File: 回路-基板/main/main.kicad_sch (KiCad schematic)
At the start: 45 parts, among them J2 Conn_01x06_Pin, Q1 PNP, Q2 NPN, Q3 PNP, Q4 NPN, SW1 SW_Push, SW2 SW_Push, SW3 SW_Push, SW4 SW_Push, SW5 SW_Push, SW6 SW_SPDT, U1 TWE-L-WX, U3 LM1117MP-3.3

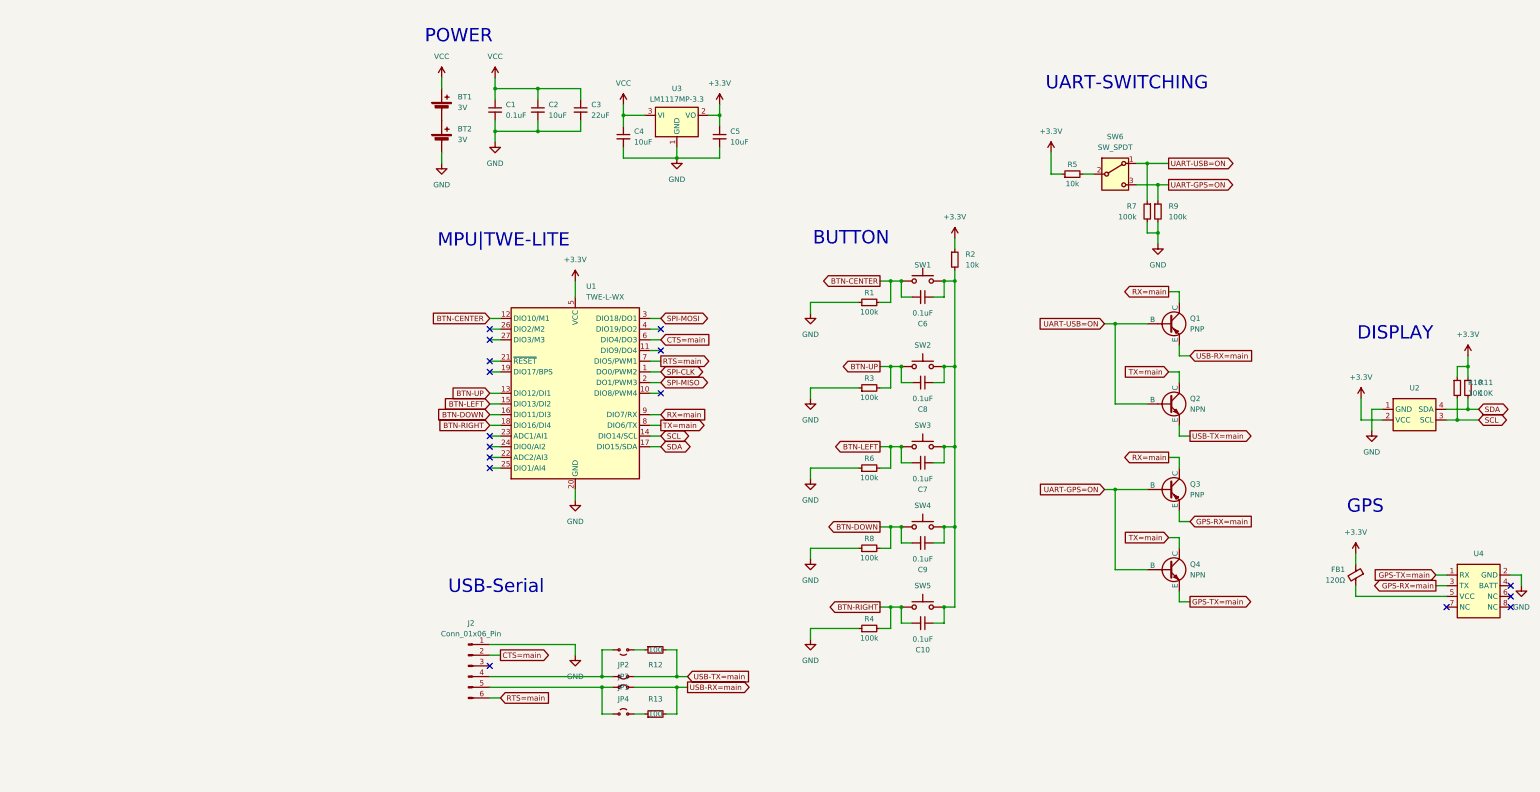
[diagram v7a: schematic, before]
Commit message: 子機基板の回路図を更新した
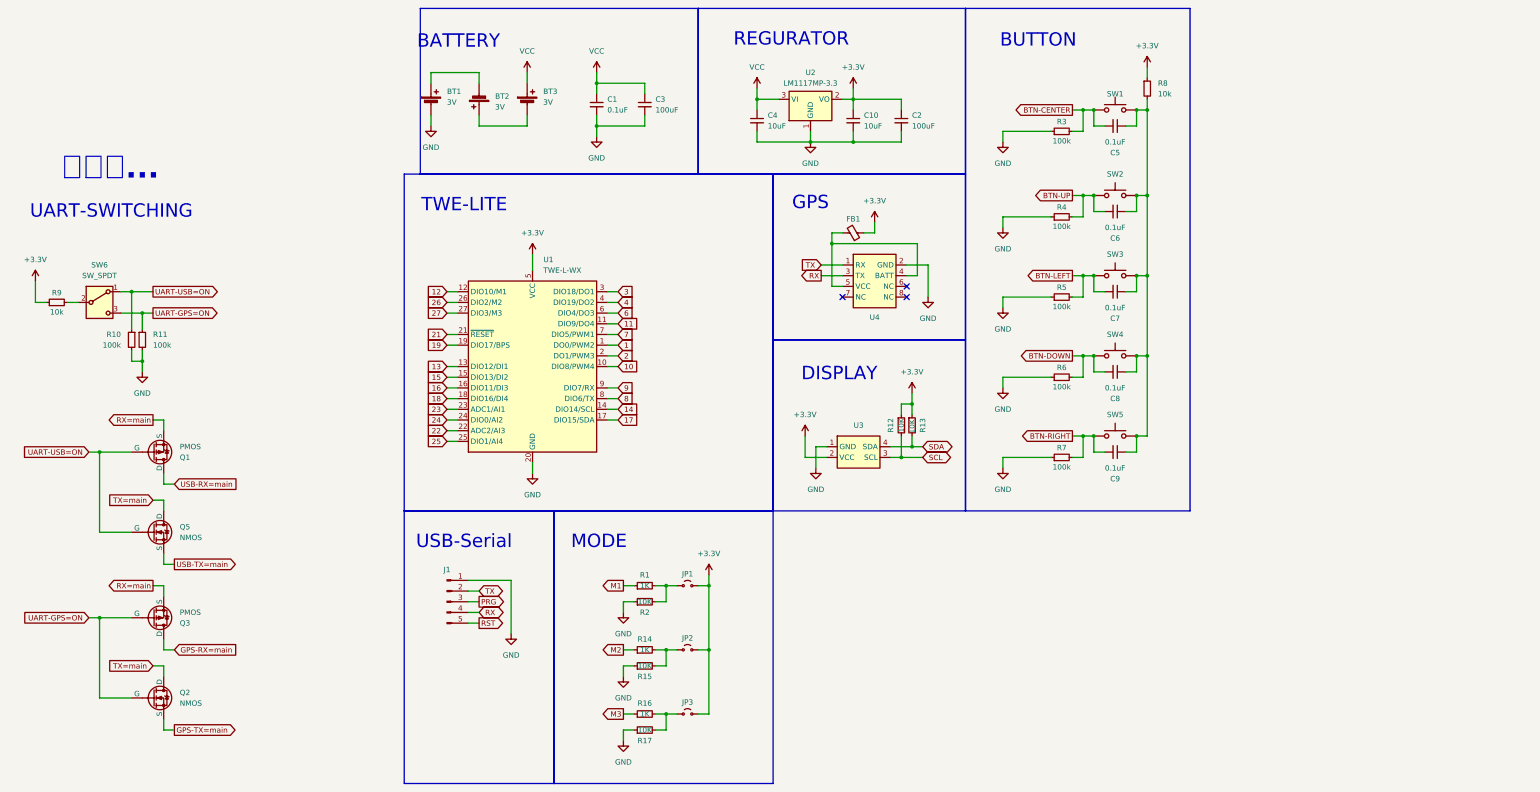
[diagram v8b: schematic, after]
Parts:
- removed J2: Conn_01x06_Pin, Connector_PinSocket_2.54mm:PinSocket_1x06_P2.54mm_Horizontal, symbol Connector:Conn_01x06_Pin
- removed JP1, JP3: Jumper_2_Small_Bridged, Jumper:SolderJumper-2_P1.3mm_Bridged_Pad1.0x1.5mm, symbol Jumper:Jumper_2_Small_Bridged
- removed JP4: Jumper_2_Small_Open, Jumper:SolderJumper-2_P1.3mm_Open_Pad1.0x1.5mm, symbol Jumper:Jumper_2_Small_Open
- removed Q1, Q3: PNP, Package_TO_SOT_SMD:SOT-323_SC-70, symbol Simulation_SPICE:PNP
- removed Q2, Q4: NPN, Package_TO_SOT_SMD:SC-59, symbol Simulation_SPICE:NPN
- removed R12, R13: 100, Resistor_SMD:R_0805_2012Metric, symbol Device:R_Small
- added BT3: 3V, @2024-cansat:BHSD-2032-SM, symbol Device:Battery_Cell
- added J1: Conn_01x05_Pin, symbol Connector:Conn_01x05_Pin
- added JP1, JP3: Jumper_2_Small_Open, symbol Jumper:Jumper_2_Small_Open
- added Q1, Q3: PMOS, symbol Simulation_SPICE:PMOS
- added Q2, Q5: NMOS, symbol Simulation_SPICE:NMOS
- added R1, R14, R16: 1K, symbol Device:R_Small
- added R15, R17, R2: 10K, symbol Device:R_Small
- C2: value 10uF -> 100uF
- C3: value 22uF -> 100uF
- FB1: value 120Ω -> FerriteBead_Small; footprint Inductor_SMD:L_0603_1608Metric -> (none)
- JP2: footprint Jumper:SolderJumper-2_P1.3mm_Open_Pad1.0x1.5mm -> (none)
- renumbered BT2 to BT1, BT1 to BT2, C5 to C10, C6 to C5, C8 to C6, C9 to C8, C10 to C9, R7 to R10, R9 to R11, R10 to R12, R11 to R13, R1 to R3, R3 to R4, R6 to R5, R8 to R6, R4 to R7, R2 to R8, R5 to R9, U3 to U2, U2 to U3
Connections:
- net +3.3V: now also C2.1, JP2.2 (B), JP1.2 (B), JP3.2 (B)
- net BTN-CENTER: no longer U1.12 (DIO10/M1)
- net BTN-DOWN: no longer U1.16 (DIO11/DI3)
- net BTN-LEFT: no longer U1.15 (DIO13/DI2)
- net BTN-RIGHT: no longer U1.18 (DIO16/DI4)
- net BTN-UP: no longer U1.13 (DIO12/DI1)
- net GND: now also J1.1 (Pin_1), R15.1, R17.1, R2.1
- net GPS-RX=main: now also Q3.1 (D); no longer U4.3 (TX)
- net GPS-TX=main: now also Q2.3 (S); no longer U4.1 (RX)
- net RX=main: now also Q1.3 (S), Q3.3 (S); no longer U1.9 (DIO7/RX)
- net SCL: no longer U1.14 (DIO14/SCL)
- net SDA: no longer U1.17 (DIO15/SDA)
- net TX=main: now also Q2.1 (D), Q5.1 (D); no longer U1.8 (DIO6/TX)
- net UART-GPS=ON: now also Q2.2 (G), Q3.2 (G)
- net UART-USB=ON: now also Q1.2 (G), Q5.2 (G)
- net USB-RX=main: now also Q1.1 (D)
- net USB-TX=main: now also Q5.3 (S)
- net VCC: now also BT3.1 (+); no longer BT2.1 (+), C2.1
- net 10: now reaches U1.10 (DIO8/PWM4)
- net 11: now reaches U1.11 (DIO9/DO4)
- net 19: now reaches U1.19 (DIO17/BPS)
- net 21: now reaches U1.21 (~{RESET})
- net 22: now reaches U1.22 (ADC2/AI3)
- net 23: now reaches U1.23 (ADC1/AI1)
- net 24: now reaches U1.24 (DIO0/AI2)
- net 25: now reaches U1.25 (DIO1/AI4)
- net 26: now reaches U1.26 (DIO2/M2)
- net 27: now reaches U1.27 (DIO3/M3)
- net 4: now reaches U1.4 (DIO19/DO2)
- net at JP2.1 (A): now also R14.2, R15.2
- net at FB1.2, U4.5 (VCC): now also U4.4 (BATT)
- net CTS=main renamed 6
- net RTS=main renamed 7
- net SPI-CLK renamed 1
- net SPI-MISO renamed 2
- net SPI-MOSI renamed 3
- new net: BT2.1 (+), BT3.2 (-)
- new net: JP1.1 (A), R1.2, R2.2
- new net: JP3.1 (A), R16.2, R17.2
- new net 12: U1.12 (DIO10/M1)
- new net 13: U1.13 (DIO12/DI1)
- new net 14: U1.14 (DIO14/SCL)
- new net 15: U1.15 (DIO13/DI2)
- new net 16: U1.16 (DIO11/DI3)
- new net 17: U1.17 (DIO15/SDA)
- new net 18: U1.18 (DIO16/DI4)
- new net 8: U1.8 (DIO6/TX)
- new net 9: U1.9 (DIO7/RX)
- new net M1: R1.1
- new net M2: R14.1
- new net M3: R16.1
- new net PRG: J1.3 (Pin_3)
- new net RST: J1.5 (Pin_5)
- new net RX: J1.4 (Pin_4), U4.3 (TX)
- new net TX: J1.2 (Pin_2), U4.1 (RX)
- no-connect marks 16 -> 3
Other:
- note added: "BATTERY"
- note added: "MODE"
- note added: "REGURATOR"
- note added: "TWE-LITE"
- note added: "考え中..."
- note removed: "MPU|TWE-LITE"
- note removed: "POWER"
- moved on the sheet: BT1, BT2, C1, C10, C3, C4, C5, C6, C7, C8, C9, R10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
